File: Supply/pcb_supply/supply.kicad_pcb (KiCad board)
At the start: 2 copper layers, 40.1 x 34 mm, 27 parts, among them J1 Screw_Terminal_01x02, J2 Screw_Terminal_01x02, Q1 FDS4685, U1 LTC3864

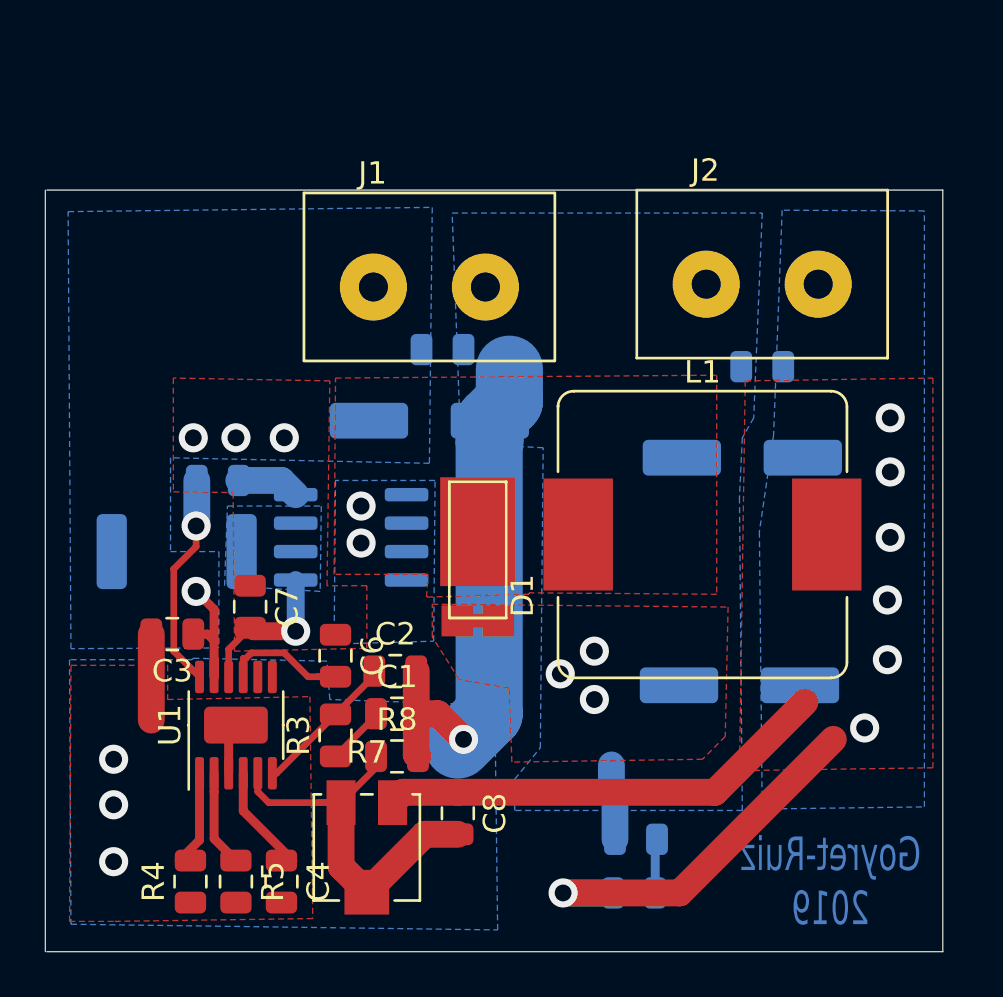
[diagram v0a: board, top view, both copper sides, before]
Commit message: Agregado de conexión Kelvin a la fuente de switching rediseñada
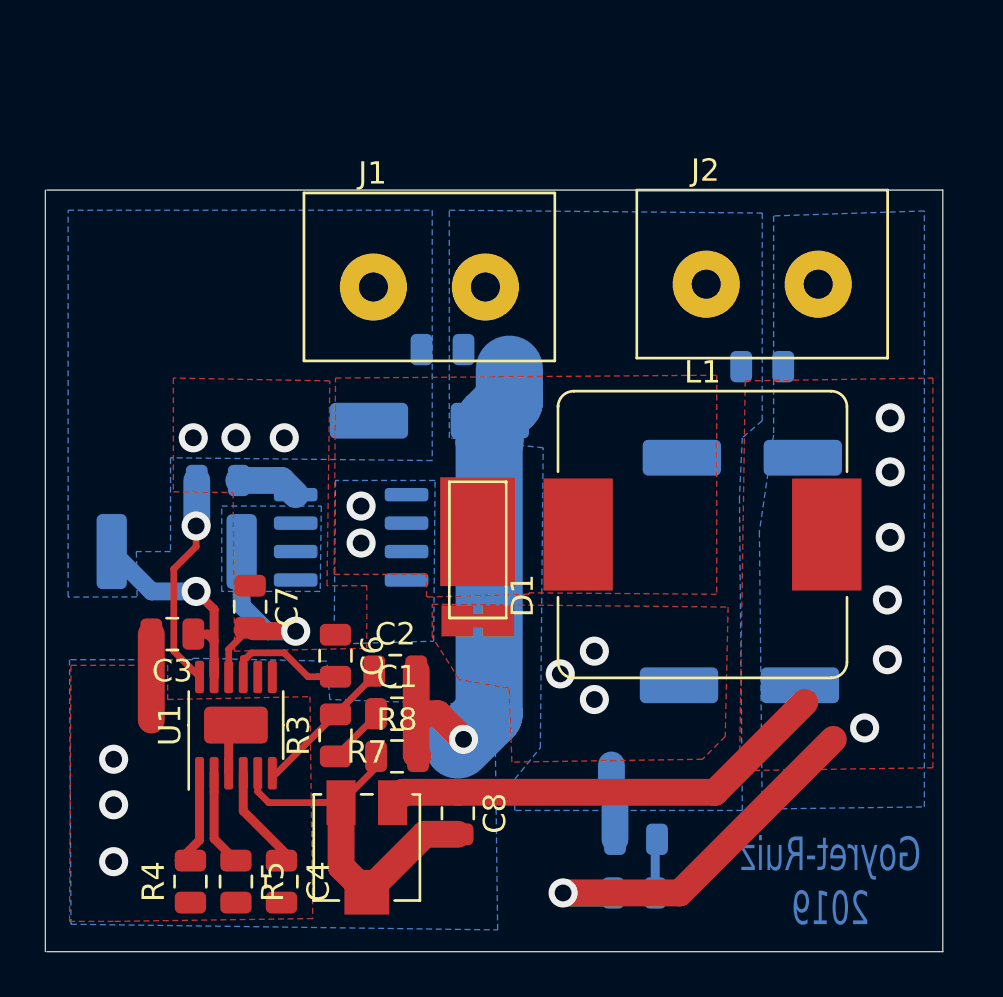
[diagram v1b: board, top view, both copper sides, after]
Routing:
- net VDC: track 5.99 -> 10.5 mm
- net Net-(C7-Pad2): track 6.98 -> 9.99 mm

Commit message: 2da version de la placa de la fuente de switching para mandar a hacer
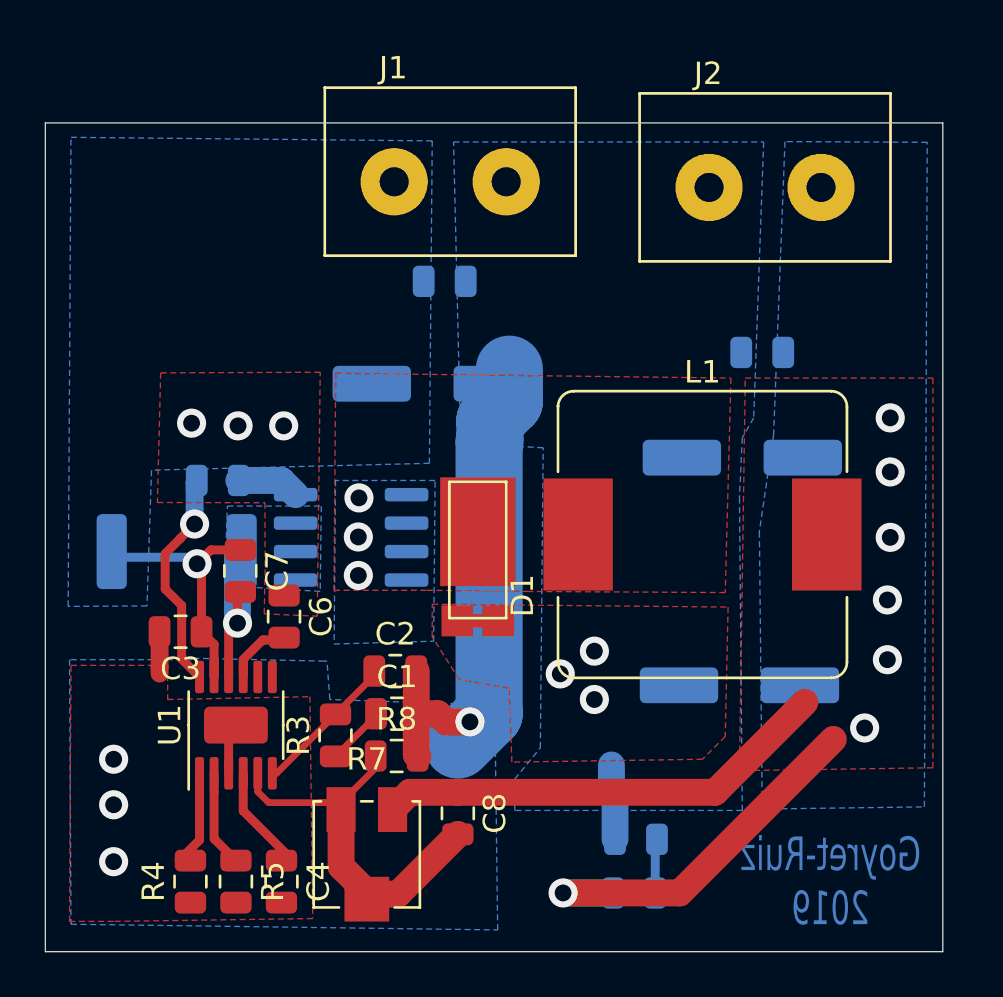
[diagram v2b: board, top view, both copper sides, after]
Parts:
- moved J1 4.79 mm to (133.0, 71.6)
- moved J2 4.32 mm to (147.1, 71.9)
- moved C12 3.05 mm to (132.8, 76.1)
- moved C6 2.89 mm to (125.6, 91.0)
- moved C7 1.66 mm to (123.6, 89.0)
- moved C5 1.66 mm to (132.2, 80.6)
- moved C9 0.63 mm to (146.9, 79.2)
- moved C3 0.38 mm to (121.0, 91.7)
- moved R7 0.31 mm to (129.3, 101.7)
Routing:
- net Net-(C6-Pad2): track 5.49 -> 2.93 mm
- net Net-(C7-Pad2): track 9.99 -> 7.81 mm
- net VDC: track 10.5 -> 12.5 mm
- net GND: track 35.4 -> 33.4 mm
- net Net-(D1-Pad1): vias 2 -> 3
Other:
- board size 40.1 x 34 mm -> 40.1 x 37 mm
